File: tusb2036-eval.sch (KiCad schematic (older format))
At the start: 48 parts, among them J1 USB_B_Micro, J2 USB_A, J3 USB_A, J4 USB_A, SW1 RESET, U1 TUSB2036, U2 TPS76333, U3 TPS2044D, U4 SN75240, U5 SN75240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

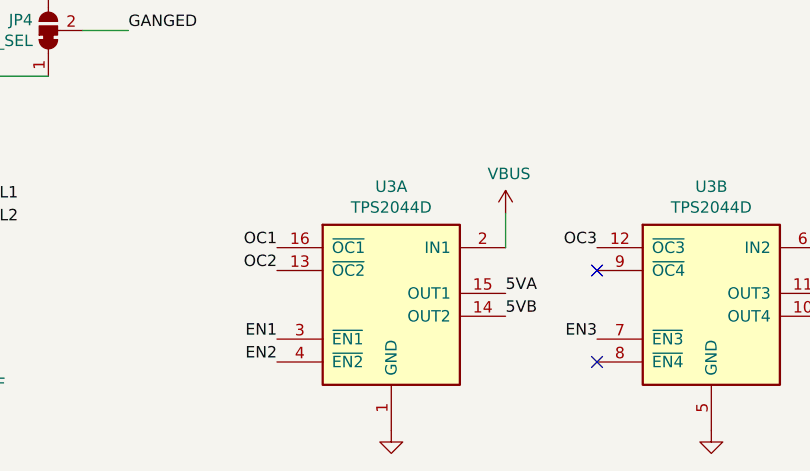
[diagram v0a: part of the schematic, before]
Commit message: Add R3 to disable TPS2044 OUT4
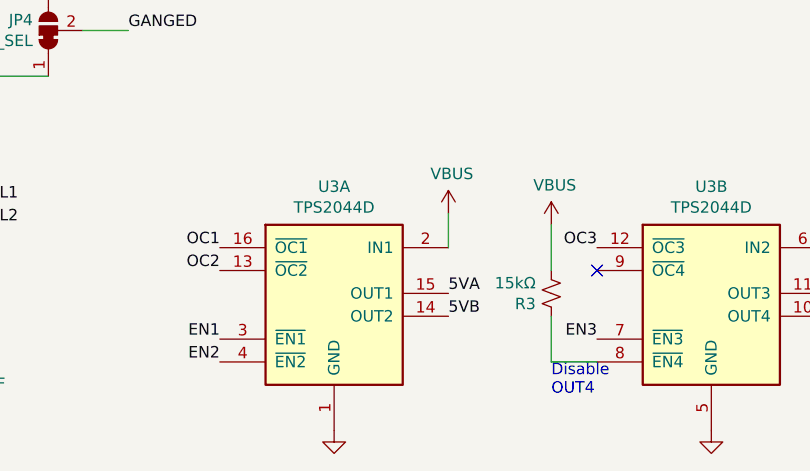
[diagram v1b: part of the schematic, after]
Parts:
- added R3: 15kΩ, Resistor_SMD:R_1206_3216Metric, symbol Device:R_Small_US
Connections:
- net VBUS: now also R3.2
- net at U3.8 (~EN4): now also R3.1
- no-connect marks 4 -> 3
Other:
- note added: "Disable\nOUT4"
- moved on the sheet: U3A
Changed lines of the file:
@@
 Title "TUSB2036 Evaluation Board"
 Date "2021-03-22"
-Rev "2"
+Rev "3"
 Comp "Chris Keller"
 Comment1 ""
@@
 L Power_Management:TPS2044D U3
 U 1 1 605F1591
-P 3800 7000
-F 0 "U3" H 3800 7467 50  0000 C CNN
-F 1 "TPS2044D" H 3800 7376 50  0000 C CNN
-F 2 "Package_SO:SOIC-16_3.9x9.9mm_P1.27mm" H 3800 7500 50  0001 C CNN
-F 3 "http://www.ti.com/lit/ds/symlink/tps2044.pdf" H 3750 7300 50  0001 C CNN
-F 4 "2.73" H 3800 7000 50  0001 C CNN "Price"
-F 5 "595-TPS2044BDR" H 3800 7000 50  0001 C CNN "Vendor Part #"
-F 6 "Mouser" H 3800 7000 50  0001 C CNN "Vendor"
-	1    3800 7000
+P 3550 7000
+F 0 "U3" H 3550 7467 50  0000 C CNN
+F 1 "TPS2044D" H 3550 7376 50  0000 C CNN
+F 2 "Package_SO:SOIC-16_3.9x9.9mm_P1.27mm" H 3550 7500 50  0001 C CNN
+F 3 "http://www.ti.com/lit/ds/symlink/tps2044.pdf" H 3500 7300 50  0001 C CNN
+F 4 "2.73" H 3550 7000 50  0001 C CNN "Price"
+F 5 "595-TPS2044BDR" H 3550 7000 50  0001 C CNN "Vendor Part #"
+F 6 "Mouser" H 3550 7000 50  0001 C CNN "Vendor"
+	1    3550 7000
 	1    0    0    -1
 $EndComp
@@
 L power:VBUS #PWR019
 U 1 1 605F85B9
-P 4300 6650
-F 0 "#PWR019" H 4300 6500 50  0001 C CNN
-F 1 "VBUS" H 4315 6823 50  0000 C CNN
-F 2 "" H 4300 6650 50  0001 C CNN
-F 3 "" H 4300 6650 50  0001 C CNN
-	1    4300 6650
+P 4050 6650
+F 0 "#PWR019" H 4050 6500 50  0001 C CNN
+F 1 "VBUS" H 4065 6823 50  0000 C CNN
+F 2 "" H 4050 6650 50  0001 C CNN
+F 3 "" H 4050 6650 50  0001 C CNN
+	1    4050 6650
 	1    0    0    -1
 $EndComp
@@
 L power:GND #PWR013
 U 1 1 6061613E
-P 3800 7600
-F 0 "#PWR013" H 3800 7350 50  0001 C CNN
-F 1 "GND" H 3805 7427 50  0001 C CNN
-F 2 "" H 3800 7600 50  0001 C CNN
-F 3 "" H 3800 7600 50  0001 C CNN
-	1    3800 7600
+P 3550 7600
+F 0 "#PWR013" H 3550 7350 50  0001 C CNN
+F 1 "GND" H 3555 7427 50  0001 C CNN
+F 2 "" H 3550 7600 50  0001 C CNN
+F 3 "" H 3550 7600 50  0001 C CNN
+	1    3550 7600
 	1    0    0    -1
 $EndComp
@@
 Text Label 9350 4800 0    50   ~ 0
 5VC
-Text Label 3300 6800 2    50   ~ 0
+Text Label 3050 6800 2    50   ~ 0
 OC1
-Text Label 3300 6900 2    50   ~ 0
+Text Label 3050 6900 2    50   ~ 0
 OC2
-Text Label 3300 7200 2    50   ~ 0
+Text Label 3050 7200 2    50   ~ 0
 EN1
-Text Label 3300 7300 2    50   ~ 0
+Text Label 3050 7300 2    50   ~ 0
 EN2
 Text Label 4700 6800 2    50   ~ 0
@@
 Text Label 4700 7200 2    50   ~ 0
 EN3
-Text Label 4300 7000 0    50   ~ 0
+Text Label 4050 7000 0    50   ~ 0
 5VA
-Text Label 4300 7100 0    50   ~ 0
+Text Label 4050 7100 0    50   ~ 0
 5VB
 Text Label 5700 7000 0    50   ~ 0
@@
 	3500 1050 3750 1050
 Wire Wire Line
-	4300 6650 4300 6800
+	4050 6650 4050 6800
 Wire Wire Line
 	5700 6800 5750 6800
@@
 NoConn ~ 5700 7100
 NoConn ~ 4700 6900
-NoConn ~ 4700 7300
 NoConn ~ 4700 4100
+$Comp
+L Device:R_Small_US R3
+U 1 1 605E5806
+P 4500 7000
+F 0 "R3" H 4568 7046 50  0000 L CNN
+F 1 "15kΩ" H 4568 6955 50  0000 L CNN
+F 2 "Resistor_SMD:R_1206_3216Metric" H 4500 7000 50  0001 C CNN
+F 3 "https://www.mouser.com/datasheet/2/447/PYu_RC_Group_51_RoHS_L_10-1664068.pdf" H 4500 7000 50  0001 C CNN
+F 4 "0.16" H 4568 7146 50  0001 C CNN "Price"
+F 5 "603-RC1210FR-0715KL" H 4568 7146 50  0001 C CNN "Vendor Part #"
+F 6 "Mouser" H 4568 7146 50  0001 C CNN "Vendor"
+	1    4500 7000
+	-1   0    0    1
+$EndComp
+$Comp
+L power:VBUS #PWR0101
+U 1 1 605E8A16
+P 4500 6700
+F 0 "#PWR0101" H 4500 6550 50  0001 C CNN
+F 1 "VBUS" H 4515 6873 50  0000 C CNN
+F 2 "" H 4500 6700 50  0001 C CNN
+F 3 "" H 4500 6700 50  0001 C CNN
+	1    4500 6700
+	1    0    0    -1
+$EndComp
+Wire Wire Line
+	4500 6700 4500 6900
+Wire Wire Line
+	4500 7100 4500 7300
+Wire Wire Line
+	4500 7300 4700 7300
+Text Notes 4500 7450 0    50   ~ 0
+Disable\nOUT4
 $EndSCHEMATC

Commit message: Fix up libraries
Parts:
- C20, C30, C40: footprint Vishay-cap:CAPPM7343X310N -> Vishay:CAPPM7343X310N
- J2, J3, J4: footprint USB-A:62900416021 -> Wurth:62900416021

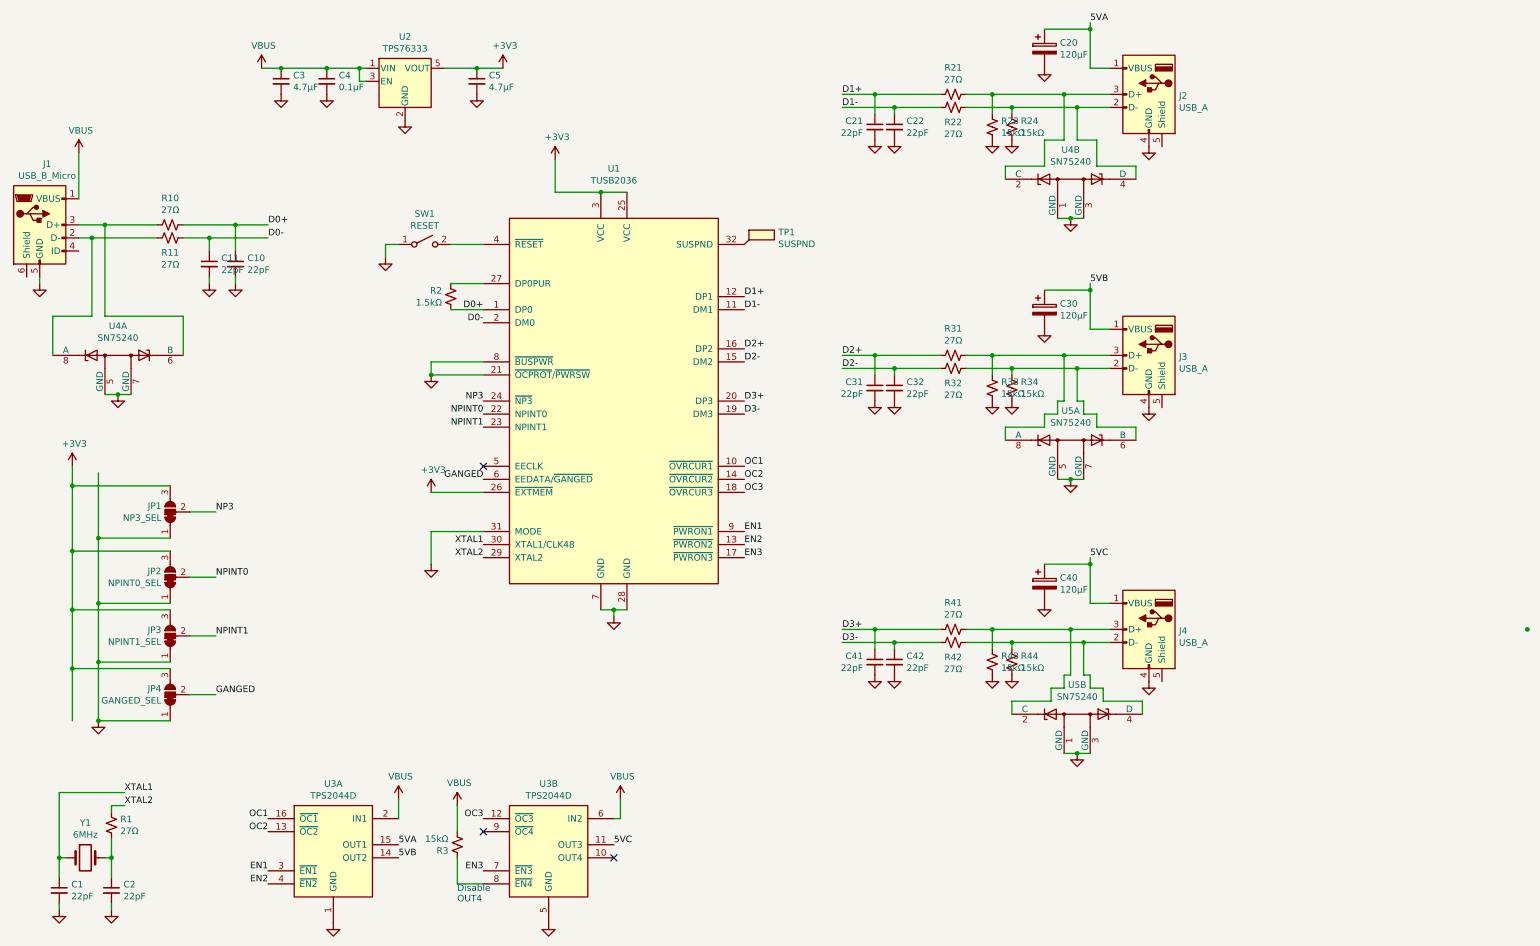
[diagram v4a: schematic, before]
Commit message: Replace micro USB connector
The Molex is difficult to hand solder, so swapping that out for the CUI
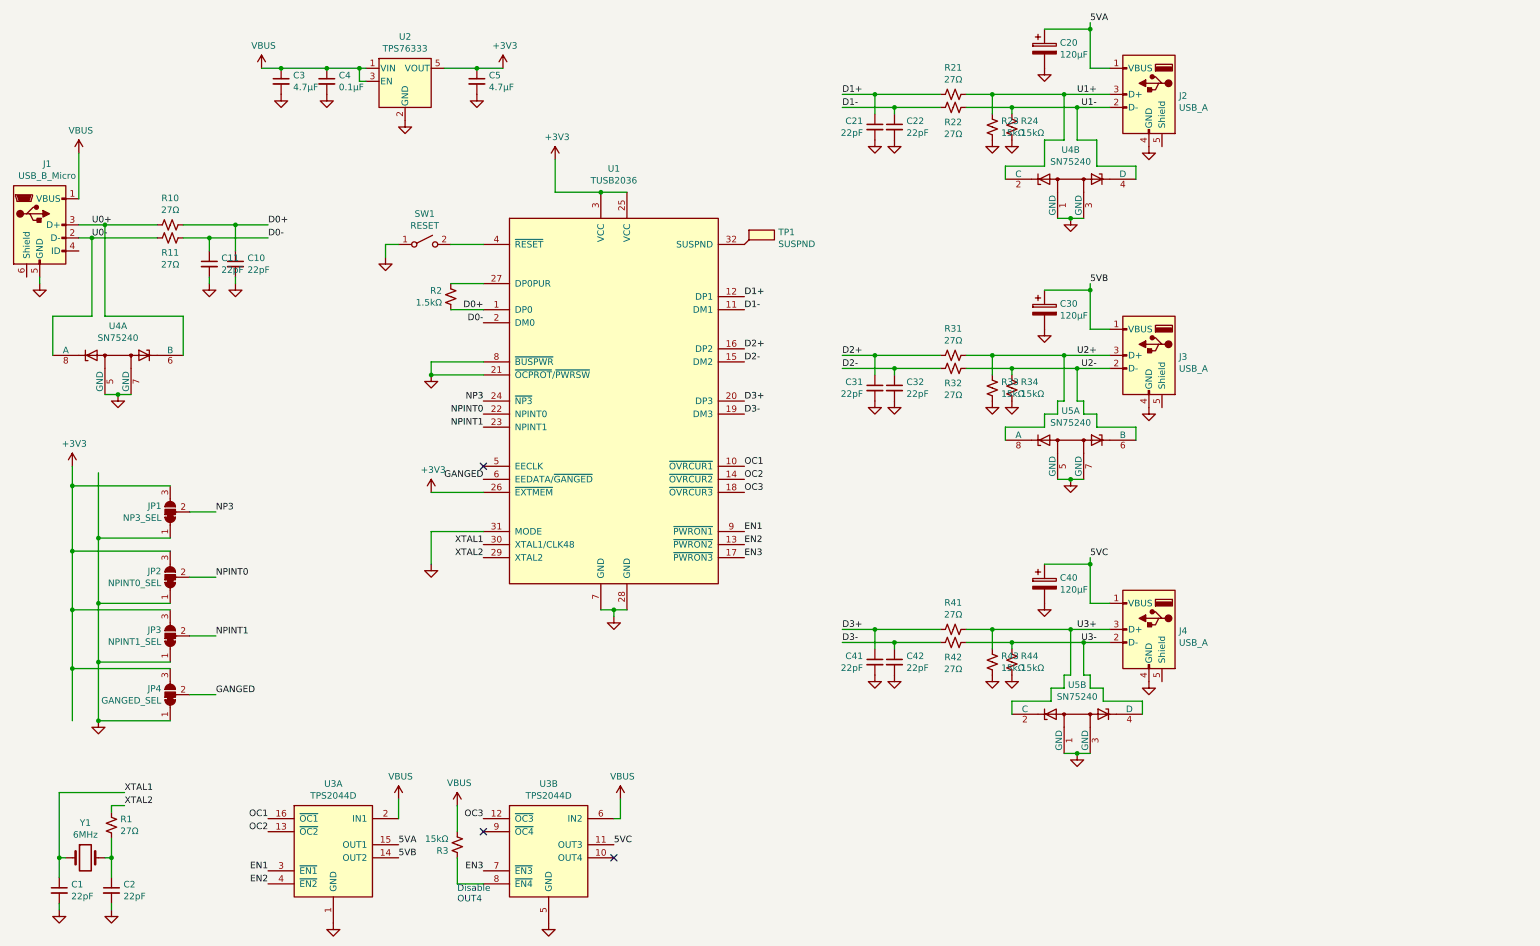
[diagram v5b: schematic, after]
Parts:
- J1: footprint Connector_USB:USB_Micro-B_Molex_47346-0001 -> CUI:UJ2-MIBH-4-SMT; Price 0.95 -> 0.79; Vendor Part # 538-47346-0001 -> 490-UJ2-MIBH-4-SMT
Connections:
- net U0-: now reaches J1.2 (D-), R11.1, U4.8 (A)
- net U0+: now reaches J1.3 (D+), R10.1, U4.6 (B)
- net U1+: now reaches J2.3 (D+), R21.2, R23.1, U4.2 (C)
- net U1-: now reaches J2.2 (D-), R22.2, R24.1, U4.4 (D)
- net U2+: now reaches J3.3 (D+), R31.2, R33.1, U5.8 (A)
- net U2-: now reaches J3.2 (D-), R32.2, R34.1, U5.6 (B)
- net U3+: now reaches J4.3 (D+), R41.2, R43.1, U5.2 (C)
- net U3-: now reaches J4.2 (D-), R42.2, R44.1, U5.4 (D)
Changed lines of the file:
@@
 Title "TUSB2036 Evaluation Board"
 Date "2021-04-14"
-Rev "3"
+Rev "4"
 Comp "Chris Keller"
 Comment1 "Licensed under Creative Commons CC-BY-4.0"
@@
 Comment4 ""
 $EndDescr
-Connection ~ 12700 5350
 Text Notes 4500 7450 0    50   ~ 0
 Disable\nOUT4
@@
 F 0 "J1" H 1357 2717 50  0000 C CNN
 F 1 "USB_B_Micro" H 1357 2626 50  0000 C CNN
-F 2 "Connector_USB:USB_Micro-B_Molex_47346-0001" H 1450 2200 50  0001 C CNN
-F 3 "https://www.mouser.com/datasheet/2/276/0473460001_IO_CONNECTORS-229243.pdf" H 1450 2200 50  0001 C CNN
-F 4 "0.95" H 1300 2250 50  0001 C CNN "Price"
-F 5 "538-47346-0001" H 1300 2250 50  0001 C CNN "Vendor Part #"
+F 2 "CUI:UJ2-MIBH-4-SMT" H 1450 2200 50  0001 C CNN
+F 3 "https://www.mouser.com/datasheet/2/670/uj2_mibh_4_smt-1313358.pdf" H 1450 2200 50  0001 C CNN
+F 4 "0.79" H 1300 2250 50  0001 C CNN "Price"
+F 5 "490-UJ2-MIBH-4-SMT" H 1300 2250 50  0001 C CNN "Vendor Part #"
 F 6 "Mouser" H 1300 2250 50  0001 C CNN "Vendor"
 	1    1300 2250
@@
 	1    0    0    -1
 $EndComp
+Text Label 1700 2250 0    50   ~ 0
+U0+
+Text Label 1700 2350 0    50   ~ 0
+U0-
+Text Label 9400 1250 2    50   ~ 0
+U1+
+Text Label 9400 1350 2    50   ~ 0
+U1-
+Text Label 9400 3250 2    50   ~ 0
+U2+
+Text Label 9400 3350 2    50   ~ 0
+U2-
+Text Label 9400 5350 2    50   ~ 0
+U3+
+Text Label 9400 5450 2    50   ~ 0
+U3-
 $EndSCHEMATC

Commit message: Add test points
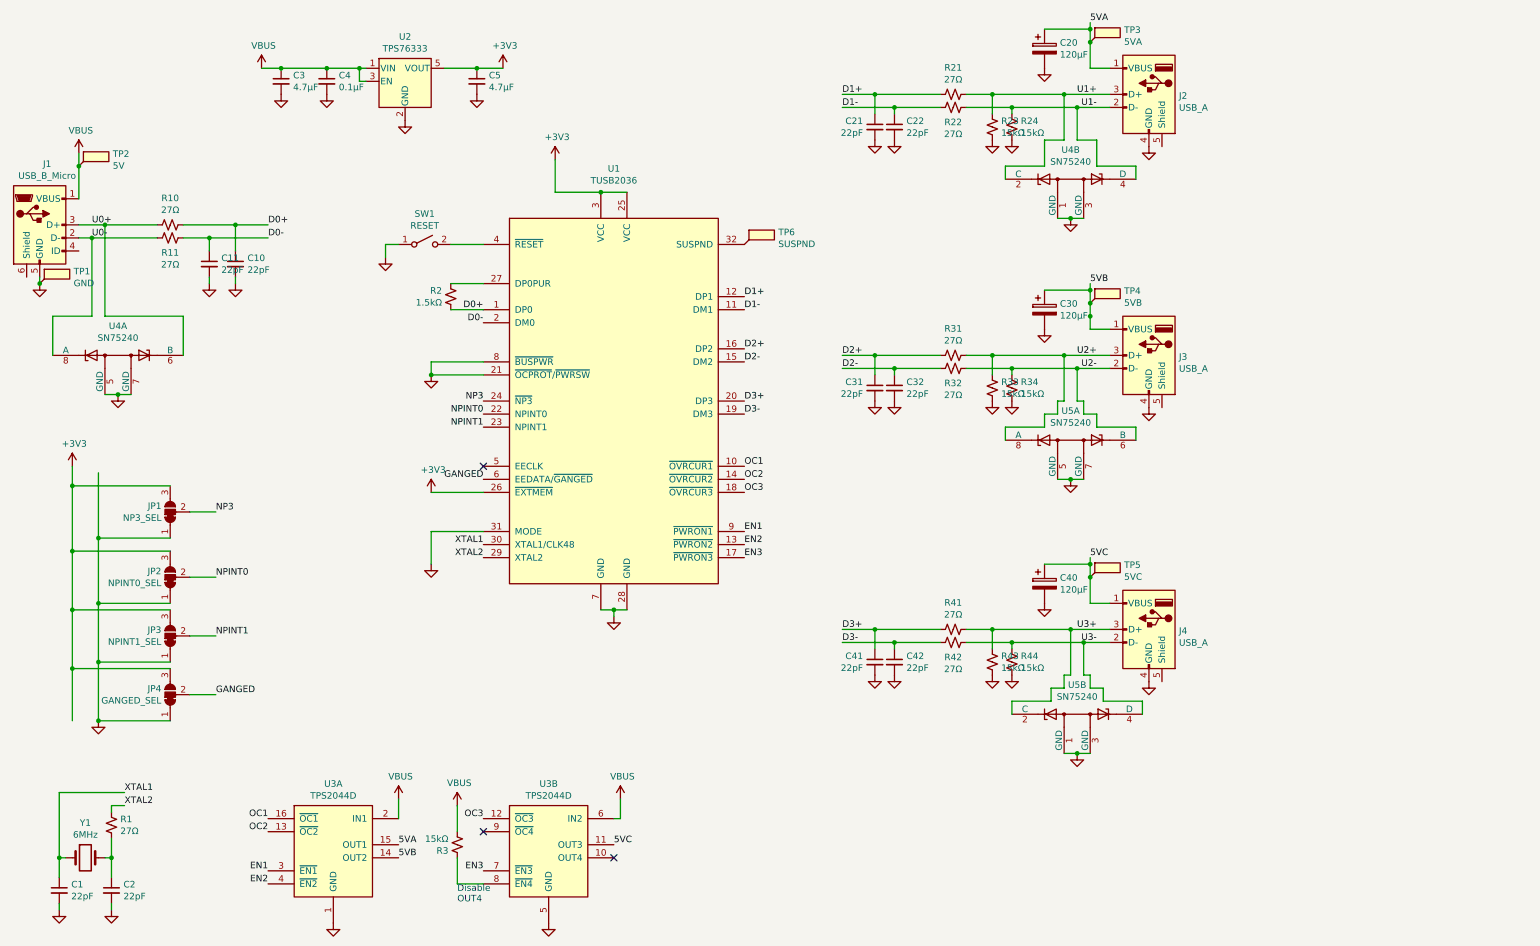
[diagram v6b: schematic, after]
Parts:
- added TP1: GND, TestPoint:TestPoint_Pad_D2.0mm, symbol Connector:TestPoint_Flag
- added TP2: 5V, TestPoint:TestPoint_Pad_D2.0mm, symbol Connector:TestPoint_Flag
- added TP3: 5VA, TestPoint:TestPoint_Pad_D2.0mm, symbol Connector:TestPoint_Flag
- added TP4: 5VB, TestPoint:TestPoint_Pad_D2.0mm, symbol Connector:TestPoint_Flag
- added TP5: 5VC, TestPoint:TestPoint_Pad_D2.0mm, symbol Connector:TestPoint_Flag
- renumbered TP1 to TP6
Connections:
- net 5VA: now also TP3.1
- net 5VB: now also TP4.1
- net 5VC: now also TP5.1
- net GND: now also TP1.1
- net VBUS: now also TP2.1
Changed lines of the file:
@@
 	9350 4850 9000 4850
 Wire Wire Line
-	9350 5150 9350 4850
+	9350 5150 9350 4950
 Wire Wire Line
 	9500 5150 9350 5150
@@
 	9350 2750 9000 2750
 Wire Wire Line
-	9350 3050 9350 2750
+	9350 3050 9350 2950
 Wire Wire Line
 	9500 3050 9350 3050
@@
 	9350 750  9000 750
 Wire Wire Line
-	9350 1050 9350 750
+	9350 1050 9350 850
 Wire Wire Line
 	9500 1050 9350 1050
@@
 	4450 2700 4700 2700
 Wire Wire Line
-	1600 1700 1600 2050
+	1600 1700 1600 1800
 Wire Wire Line
 	1800 2250 2200 2250
@@
 $EndComp
 $Comp
-L Connector:TestPoint_Flag TP1
+L Connector:TestPoint_Flag TP6
 U 1 1 609425DF
 P 6700 2400
-F 0 "TP1" H 6960 2494 50  0000 L CNN
+F 0 "TP6" H 6960 2494 50  0000 L CNN
 F 1 "SUSPND" H 6960 2403 50  0000 L CNN
 F 2 "TestPoint:TestPoint_Pad_D2.0mm" H 6900 2400 50  0001 C CNN
@@
 Text Label 9400 5450 2    50   ~ 0
 U3-
+$Comp
+L Connector:TestPoint_Flag TP2
+U 1 1 607984F9
+P 1600 1800
+F 0 "TP2" H 1860 1894 50  0000 L CNN
+F 1 "5V" H 1860 1803 50  0000 L CNN
+F 2 "TestPoint:TestPoint_Pad_D2.0mm" H 1800 1800 50  0001 C CNN
+F 3 "~" H 1800 1800 50  0001 C CNN
+	1    1600 1800
+	1    0    0    -1
+$EndComp
+Connection ~ 1600 1800
+Wire Wire Line
+	1600 1800 1600 2050
+$Comp
+L Connector:TestPoint_Flag TP1
+U 1 1 60799622
+P 1300 2700
+F 0 "TP1" H 1560 2794 50  0000 L CNN
+F 1 "GND" H 1560 2703 50  0000 L CNN
+F 2 "TestPoint:TestPoint_Pad_D2.0mm" H 1500 2700 50  0001 C CNN
+F 3 "~" H 1500 2700 50  0001 C CNN
+	1    1300 2700
+	1    0    0    -1
+$EndComp
+Connection ~ 1300 2700
+$Comp
+L Connector:TestPoint_Flag TP3
+U 1 1 6079A23E
+P 9350 850
+F 0 "TP3" H 9610 944 50  0000 L CNN
+F 1 "5VA" H 9610 853 50  0000 L CNN
+F 2 "TestPoint:TestPoint_Pad_D2.0mm" H 9550 850 50  0001 C CNN
+F 3 "~" H 9550 850 50  0001 C CNN
+	1    9350 850
+	1    0    0    -1
+$EndComp
+Connection ~ 9350 850
+Wire Wire Line
+	9350 850  9350 750
+$Comp
+L Connector:TestPoint_Flag TP4
+U 1 1 6079ACE3
+P 9350 2850
+F 0 "TP4" H 9610 2944 50  0000 L CNN
+F 1 "5VB" H 9610 2853 50  0000 L CNN
+F 2 "TestPoint:TestPoint_Pad_D2.0mm" H 9550 2850 50  0001 C CNN
+F 3 "~" H 9550 2850 50  0001 C CNN
+	1    9350 2850
+	1    0    0    -1
+$EndComp
+Connection ~ 9350 2950
+Wire Wire Line
+	9350 2950 9350 2850
+Connection ~ 9350 2850
+Wire Wire Line
+	9350 2850 9350 2750
+$Comp
+L Connector:TestPoint_Flag TP5
+U 1 1 6079B705
+P 9350 4950
+F 0 "TP5" H 9610 5044 50  0000 L CNN
+F 1 "5VC" H 9610 4953 50  0000 L CNN
+F 2 "TestPoint:TestPoint_Pad_D2.0mm" H 9550 4950 50  0001 C CNN
+F 3 "~" H 9550 4950 50  0001 C CNN
+	1    9350 4950
+	1    0    0    -1
+$EndComp
+Connection ~ 9350 4950
+Wire Wire Line
+	9350 4950 9350 4850
 $EndSCHEMATC

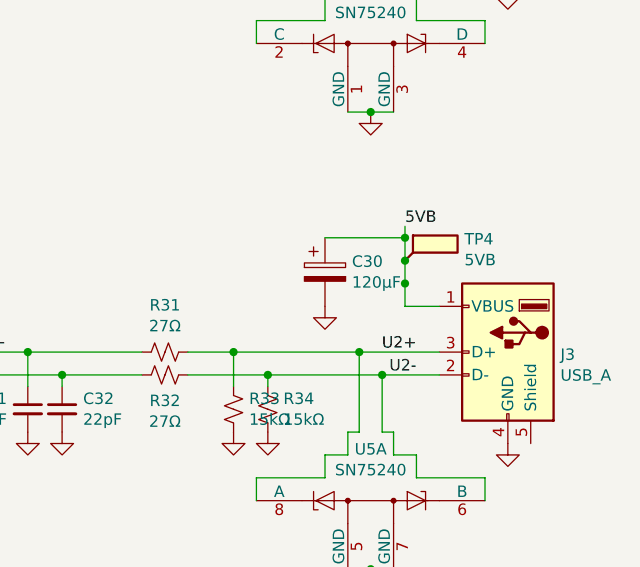
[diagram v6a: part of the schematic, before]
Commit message: Fix button footprint and other small updates
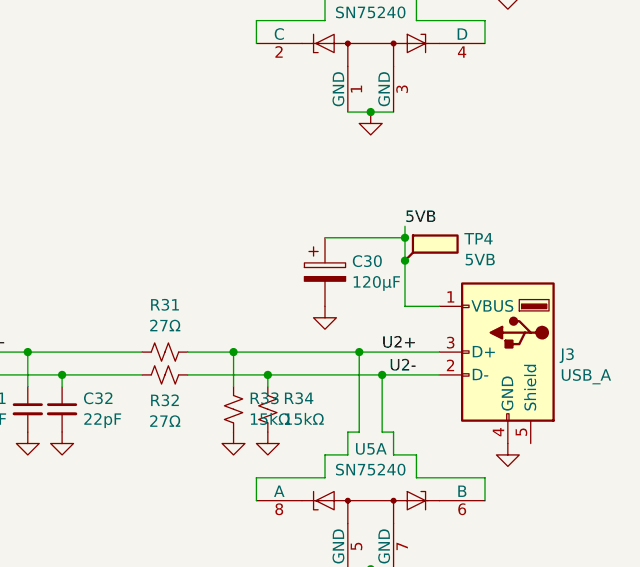
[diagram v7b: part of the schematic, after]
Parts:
- SW1: footprint Button_Switch_SMD:SW_SPST_Omron_B3FS-100xP -> Omron:SW_SPST_Omron_B3FS-100xP
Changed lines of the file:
@@
 Sheet 1 1
 Title "TUSB2036 Evaluation Board"
-Date "2021-04-14"
+Date "2021-04-18"
 Rev "4"
 Comp "Chris Keller"
@@
 Wire Wire Line
 	9350 2750 9000 2750
-Wire Wire Line
-	9350 3050 9350 2950
 Wire Wire Line
 	9500 3050 9350 3050
@@
 F 0 "SW1" H 4250 2635 50  0000 C CNN
 F 1 "RESET" H 4250 2544 50  0000 C CNN
-F 2 "Button_Switch_SMD:SW_SPST_Omron_B3FS-100xP" H 4250 2400 50  0001 C CNN
+F 2 "Omron:SW_SPST_Omron_B3FS-100xP" H 4250 2400 50  0001 C CNN
 F 3 "https://www.mouser.com/datasheet/2/307/omron_B3FS-1189765.pdf" H 4250 2400 50  0001 C CNN
 F 4 "0.58" H 4250 2735 50  0001 C CNN "Price"
@@
 	1    0    0    -1
 $EndComp
-Connection ~ 9350 2950
-Wire Wire Line
-	9350 2950 9350 2850
 Connection ~ 9350 2850
 Wire Wire Line
@@
 Wire Wire Line
 	9350 4950 9350 4850
+Wire Wire Line
+	9350 2850 9350 3050
 $EndSCHEMATC
